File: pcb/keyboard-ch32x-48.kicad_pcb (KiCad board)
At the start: 2 copper layers, 224.6 x 74.2 mm, 116 parts, among them J1 USB_C_Receptacle_USB2.0, J2 Conn_01x02, J3 Conn_01x04, SW1 SW_SPST, SW2 SW_SPST, U1 CH32X033F8P6

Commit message: pcb: ch32x-48: rev2025.2
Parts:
- added C3: 4.7uF, Capacitor_SMD:C_0805_2012Metric, B.Cu at (154.7, 64.5)
- turned D_1_1 to -90 degrees
- turned D_1_2 to -90 degrees
- turned D_1_3 to -90 degrees
- turned D_1_4 to -90 degrees
- turned D_1_5 to -90 degrees
- turned D_1_6 to -90 degrees
- turned D_1_7 to -90 degrees
- turned D_2_1 to -90 degrees
- turned D_2_2 to -90 degrees
- turned D_2_3 to -90 degrees
- turned D_2_4 to -90 degrees
- turned D_2_5 to -90 degrees
- turned D_2_6 to -90 degrees
- turned D_2_7 to -90 degrees
- turned D_3_1 to -90 degrees
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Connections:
- D_1_1 pad 1: /ROW1 -> Net-(D_1_1-K)
- D_1_1 pad 2: Net-(D_1_1-A) -> /ROW1
- D_1_2 pad 1: /ROW1 -> Net-(D_1_2-K)
- D_1_2 pad 2: Net-(D_1_2-A) -> /ROW1
- D_1_3 pad 1: /ROW1 -> Net-(D_1_3-K)
- D_1_3 pad 2: Net-(D_1_3-A) -> /ROW1
- D_1_4 pad 1: /ROW1 -> Net-(D_1_4-K)
- D_1_4 pad 2: Net-(D_1_4-A) -> /ROW1
- D_1_5 pad 1: /ROW1 -> Net-(D_1_5-K)
- D_1_5 pad 2: Net-(D_1_5-A) -> /ROW1
- D_1_6 pad 1: /ROW1 -> Net-(D_1_6-K)
- D_1_6 pad 2: Net-(D_1_6-A) -> /ROW1
- D_1_7 pad 1: /ROW1 -> Net-(D_1_7-K)
- D_1_7 pad 2: Net-(D_1_7-A) -> /ROW1
- D_2_1 pad 1: /DCK -> Net-(D_2_1-K)
- D_2_1 pad 2: Net-(D_2_1-A) -> /DCK
- D_2_2 pad 1: /DCK -> Net-(D_2_2-K)
- D_2_2 pad 2: Net-(D_2_2-A) -> /DCK
- D_2_3 pad 1: /DCK -> Net-(D_2_3-K)
- D_2_3 pad 2: Net-(D_2_3-A) -> /DCK
- D_2_4 pad 1: /DCK -> Net-(D_2_4-K)
- D_2_4 pad 2: Net-(D_2_4-A) -> /DCK
- D_2_5 pad 1: /DCK -> Net-(D_2_5-K)
- D_2_5 pad 2: Net-(D_2_5-A) -> /DCK
- D_2_6 pad 1: /DCK -> Net-(D_2_6-K)
- D_2_6 pad 2: Net-(D_2_6-A) -> /DCK
- D_2_7 pad 1: /DCK -> Net-(D_2_7-K)
- D_2_7 pad 2: Net-(D_2_7-A) -> /DCK
- D_3_1 pad 1: /ROW3 -> Net-(D_3_1-K)
- D_3_1 pad 2: Net-(D_3_1-A) -> /ROW3
- D_3_2 pad 1: /ROW3 -> Net-(D_3_2-K)
- D_3_2 pad 2: Net-(D_3_2-A) -> /ROW3
- D_3_3 pad 1: /ROW3 -> Net-(D_3_3-K)
- D_3_3 pad 2: Net-(D_3_3-A) -> /ROW3
- D_3_4 pad 1: /ROW3 -> Net-(D_3_4-K)
- D_3_4 pad 2: Net-(D_3_4-A) -> /ROW3
- D_3_5 pad 1: /ROW3 -> Net-(D_3_5-K)
- D_3_5 pad 2: Net-(D_3_5-A) -> /ROW3
- D_3_6 pad 1: /ROW3 -> Net-(D_3_6-K)
- D_3_6 pad 2: Net-(D_3_6-A) -> /ROW3
- D_3_7 pad 1: /ROW3 -> Net-(D_3_7-K)
- D_3_7 pad 2: Net-(D_3_7-A) -> /ROW3
- D_4_1 pad 1: /ROW4 -> Net-(D_4_1-K)
- D_4_1 pad 2: Net-(D_4_1-A) -> /ROW4
- D_4_2 pad 1: /ROW4 -> Net-(D_4_2-K)
- D_4_2 pad 2: Net-(D_4_2-A) -> /ROW4
- D_4_3 pad 1: /ROW4 -> Net-(D_4_3-K)
- D_4_3 pad 2: Net-(D_4_3-A) -> /ROW4
- D_4_4 pad 1: /ROW4 -> Net-(D_4_4-K)
- D_4_4 pad 2: Net-(D_4_4-A) -> /ROW4
- D_4_5 pad 1: /ROW4 -> Net-(D_4_5-K)
- D_4_5 pad 2: Net-(D_4_5-A) -> /ROW4
- D_4_6 pad 1: /ROW4 -> Net-(D_4_6-K)
- D_4_6 pad 2: Net-(D_4_6-A) -> /ROW4
- D_4_7 pad 1: /ROW4 -> Net-(D_4_7-K)
- D_4_7 pad 2: Net-(D_4_7-A) -> /ROW4
- D_5_1 pad 1: /ROW5 -> Net-(D_5_1-K)
- D_5_1 pad 2: Net-(D_5_1-A) -> /ROW5
- D_5_2 pad 1: /ROW5 -> Net-(D_5_2-K)
- D_5_2 pad 2: Net-(D_5_2-A) -> /ROW5
- D_5_3 pad 1: /ROW5 -> Net-(D_5_3-K)
- D_5_3 pad 2: Net-(D_5_3-A) -> /ROW5
- D_5_4 pad 1: /ROW5 -> Net-(D_5_4-K)
- D_5_4 pad 2: Net-(D_5_4-A) -> /ROW5
- D_5_5 pad 1: /ROW5 -> Net-(D_5_5-K)
- D_5_5 pad 2: Net-(D_5_5-A) -> /ROW5
- D_5_6 pad 1: /ROW5 -> Net-(D_5_6-K)
- D_5_6 pad 2: Net-(D_5_6-A) -> /ROW5
- D_5_7 pad 1: /ROW5 -> Net-(D_5_7-K)
- D_5_7 pad 2: Net-(D_5_7-A) -> /ROW5
- D_6_1 pad 1: /DIO -> Net-(D_6_1-K)
- D_6_1 pad 2: Net-(D_6_1-A) -> /DIO
- D_6_2 pad 1: /DIO -> Net-(D_6_2-K)
- D_6_2 pad 2: Net-(D_6_2-A) -> /DIO
- D_6_3 pad 1: /DIO -> Net-(D_6_3-K)
- D_6_3 pad 2: Net-(D_6_3-A) -> /DIO
- D_6_4 pad 1: /DIO -> Net-(D_6_4-K)
- D_6_4 pad 2: Net-(D_6_4-A) -> /DIO
- D_6_5 pad 1: /DIO -> Net-(D_6_5-K)
- D_6_5 pad 2: Net-(D_6_5-A) -> /DIO
- D_6_6 pad 1: /DIO -> Net-(D_6_6-K)
- D_6_6 pad 2: Net-(D_6_6-A) -> /DIO
- D_6_7 pad 1: /DIO -> Net-(D_6_7-K)
- D_6_7 pad 2: Net-(D_6_7-A) -> /DIO
- D_7_1 pad 1: /ROW7 -> Net-(D_7_1-K)
- D_7_1 pad 2: Net-(D_7_1-A) -> /ROW7
- D_7_2 pad 1: /ROW7 -> Net-(D_7_2-K)
- D_7_2 pad 2: Net-(D_7_2-A) -> /ROW7
- D_7_3 pad 1: /ROW7 -> Net-(D_7_3-K)
- D_7_3 pad 2: Net-(D_7_3-A) -> /ROW7
- D_7_4 pad 1: /ROW7 -> Net-(D_7_4-K)
- D_7_4 pad 2: Net-(D_7_4-A) -> /ROW7
- D_7_5 pad 1: /ROW7 -> Net-(D_7_5-K)
- D_7_5 pad 2: Net-(D_7_5-A) -> /ROW7
- D_7_6 pad 1: /ROW7 -> Net-(D_7_6-K)
- D_7_6 pad 2: Net-(D_7_6-A) -> /ROW7
- SW_1_1 pad 2: Net-(D_1_1-A) -> Net-(D_1_1-K)
- SW_1_2 pad 2: Net-(D_1_2-A) -> Net-(D_1_2-K)
- SW_1_3 pad 2: Net-(D_1_3-A) -> Net-(D_1_3-K)
- SW_1_4 pad 2: Net-(D_1_4-A) -> Net-(D_1_4-K)
- SW_1_5 pad 2: Net-(D_1_5-A) -> Net-(D_1_5-K)
- SW_1_6 pad 2: Net-(D_1_6-A) -> Net-(D_1_6-K)
- SW_1_7 pad 2: Net-(D_1_7-A) -> Net-(D_1_7-K)
- SW_2_1 pad 2: Net-(D_2_1-A) -> Net-(D_2_1-K)
- SW_2_2 pad 2: Net-(D_2_2-A) -> Net-(D_2_2-K)
- SW_2_3 pad 2: Net-(D_2_3-A) -> Net-(D_2_3-K)
- SW_2_4 pad 2: Net-(D_2_4-A) -> Net-(D_2_4-K)
- SW_2_5 pad 2: Net-(D_2_5-A) -> Net-(D_2_5-K)
- SW_2_6 pad 2: Net-(D_2_6-A) -> Net-(D_2_6-K)
- SW_2_7 pad 2: Net-(D_2_7-A) -> Net-(D_2_7-K)
- SW_3_1 pad 2: Net-(D_3_1-A) -> Net-(D_3_1-K)
- SW_3_2 pad 2: Net-(D_3_2-A) -> Net-(D_3_2-K)
- SW_3_3 pad 2: Net-(D_3_3-A) -> Net-(D_3_3-K)
- SW_3_4 pad 2: Net-(D_3_4-A) -> Net-(D_3_4-K)
- SW_3_5 pad 2: Net-(D_3_5-A) -> Net-(D_3_5-K)
- SW_3_6 pad 2: Net-(D_3_6-A) -> Net-(D_3_6-K)
- SW_3_7 pad 2: Net-(D_3_7-A) -> Net-(D_3_7-K)
- SW_4_1 pad 2: Net-(D_4_1-A) -> Net-(D_4_1-K)
- SW_4_2 pad 2: Net-(D_4_2-A) -> Net-(D_4_2-K)
- SW_4_3 pad 2: Net-(D_4_3-A) -> Net-(D_4_3-K)
- SW_4_4 pad 2: Net-(D_4_4-A) -> Net-(D_4_4-K)
- SW_4_5 pad 2: Net-(D_4_5-A) -> Net-(D_4_5-K)
- SW_4_6 pad 2: Net-(D_4_6-A) -> Net-(D_4_6-K)
- SW_4_7 pad 2: Net-(D_4_7-A) -> Net-(D_4_7-K)
- SW_5_1 pad 2: Net-(D_5_1-A) -> Net-(D_5_1-K)
- SW_5_2 pad 2: Net-(D_5_2-A) -> Net-(D_5_2-K)
- SW_5_3 pad 2: Net-(D_5_3-A) -> Net-(D_5_3-K)
- SW_5_4 pad 2: Net-(D_5_4-A) -> Net-(D_5_4-K)
- SW_5_5 pad 2: Net-(D_5_5-A) -> Net-(D_5_5-K)
- SW_5_6 pad 2: Net-(D_5_6-A) -> Net-(D_5_6-K)
- SW_5_7 pad 2: Net-(D_5_7-A) -> Net-(D_5_7-K)
- SW_6_1 pad 2: Net-(D_6_1-A) -> Net-(D_6_1-K)
- SW_6_2 pad 2: Net-(D_6_2-A) -> Net-(D_6_2-K)
- SW_6_3 pad 2: Net-(D_6_3-A) -> Net-(D_6_3-K)
- SW_6_4 pad 2: Net-(D_6_4-A) -> Net-(D_6_4-K)
- SW_6_5 pad 2: Net-(D_6_5-A) -> Net-(D_6_5-K)
- SW_6_6 pad 2: Net-(D_6_6-A) -> Net-(D_6_6-K)
- SW_6_7 pad 2: Net-(D_6_7-A) -> Net-(D_6_7-K)
- SW_7_1 pad 2: Net-(D_7_1-A) -> Net-(D_7_1-K)
- SW_7_2 pad 2: Net-(D_7_2-A) -> Net-(D_7_2-K)
- SW_7_3 pad 2: Net-(D_7_3-A) -> Net-(D_7_3-K)
- SW_7_4 pad 2: Net-(D_7_4-A) -> Net-(D_7_4-K)
- SW_7_5 pad 2: Net-(D_7_5-A) -> Net-(D_7_5-K)
- SW_7_6 pad 2: Net-(D_7_6-A) -> Net-(D_7_6-K)
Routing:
- net Net-(D_2_4-K): track 0.00 -> 14.5 mm
- net Net-(D_2_4-A): track 14.5 -> 0.00 mm
- net Net-(D_7_3-K): track 0.00 -> 12.1 mm
- net Net-(D_7_3-A): track 12.1 -> 0.00 mm
- net Net-(D_2_5-K): track 0.00 -> 12.1 mm
- net Net-(D_2_5-A): track 12.1 -> 0.00 mm
- net Net-(D_1_4-K): track 0.00 -> 12.1 mm
- net Net-(D_1_4-A): track 12.1 -> 0.00 mm
- net Net-(D_1_3-K): track 0.00 -> 12.1 mm
- net Net-(D_1_3-A): track 12.1 -> 0.00 mm
- net Net-(D_1_2-K): track 0.00 -> 12.1 mm
- net Net-(D_1_2-A): track 12.1 -> 0.00 mm
- net Net-(D_6_2-K): track 0.00 -> 12.1 mm
- net Net-(D_6_2-A): track 12.1 -> 0.00 mm
- net Net-(D_5_1-K): track 0.00 -> 12.1 mm
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
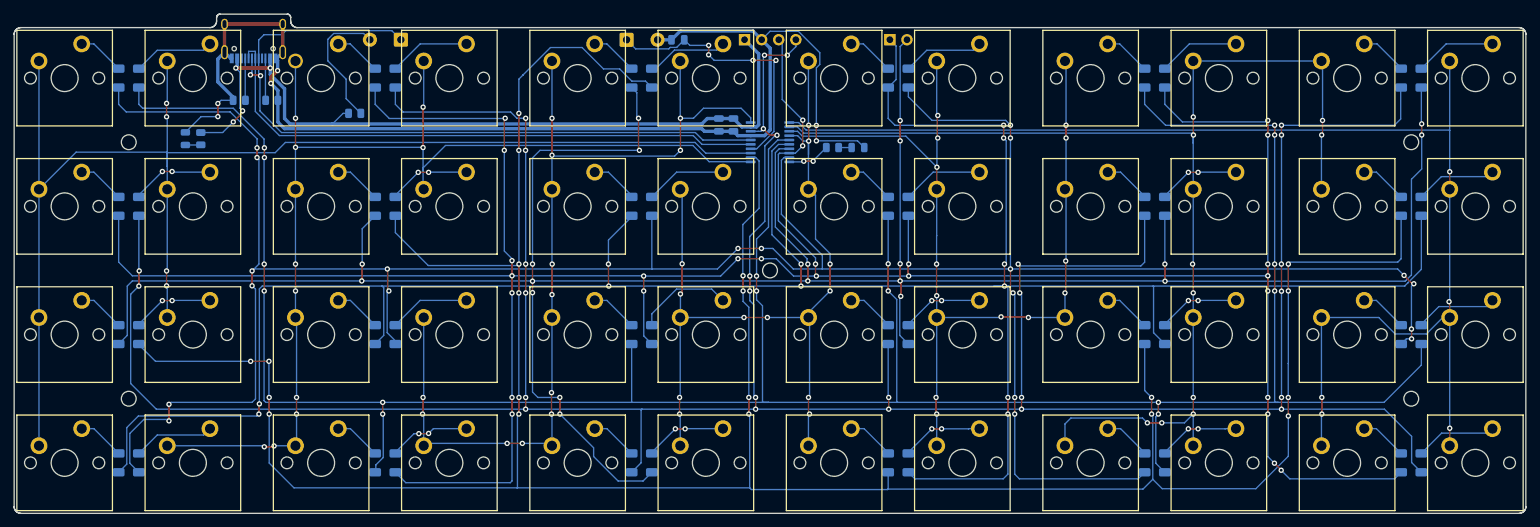
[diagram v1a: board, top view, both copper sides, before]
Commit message: pcb: ch32x-48 rev2025.3
rev2025.3:
- increase trace width to 0.25,
  - fix DRC.
- add 10K pullup for Row6 (DIO),
   per testing of the rev2025.1 board.

rev2025.2:
- fixed the diodes to be col2row,
  as the assignments of rows
  (and CH32X limitations on pins)
  required this.
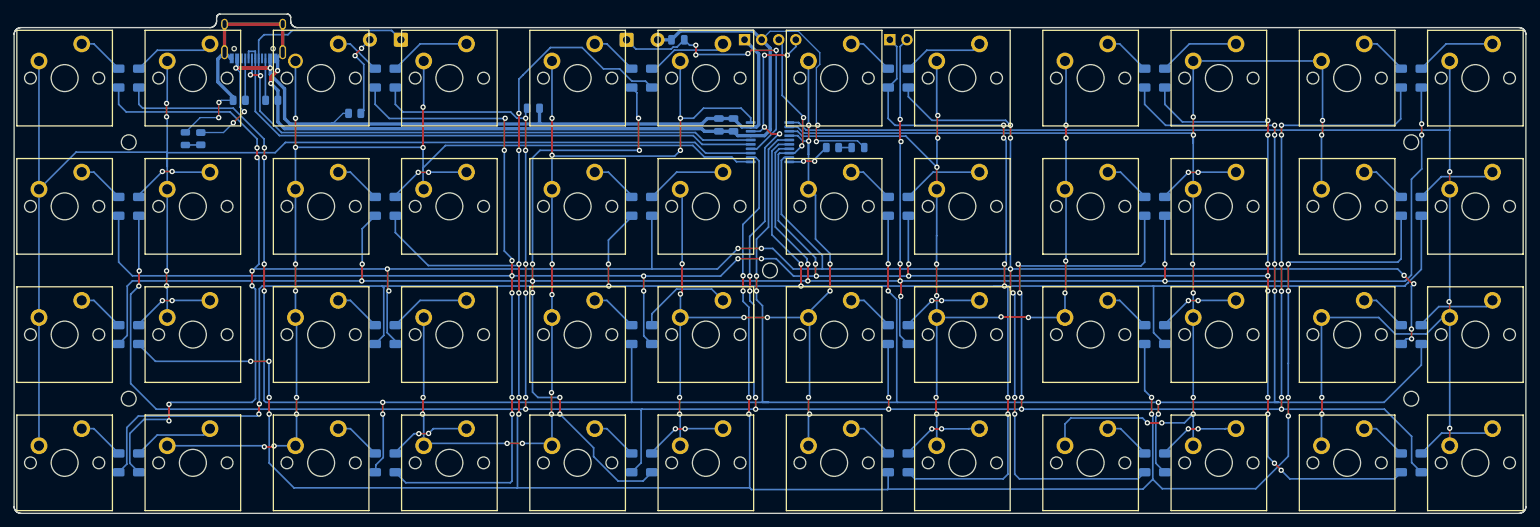
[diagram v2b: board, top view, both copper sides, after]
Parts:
- added R6: 10K, Resistor_SMD:R_0805_2012Metric, B.Cu at (127.1, 62.0)
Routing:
- net Net-(SW2-B): track 20.0 -> 12.6 mm, vias 0 -> 2
- net /VDD: track 119.2 -> 121.9 mm
- net /DIO: track 487.8 -> 490.0 mm
- net /RESET: track 40.6 -> 42.2 mm

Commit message: pcb: ch32x-48 rev2025.4
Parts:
- removed R6: 10K, Resistor_SMD:R_0805_2012Metric
- SW_1_1, SW_1_2, SW_1_3, SW_1_4, SW_1_5, SW_1_6, SW_1_7, SW_2_1, SW_2_2, SW_2_3, SW_2_4, SW_2_5, SW_2_6, SW_2_7, SW_3_1, SW_3_2, SW_3_3, SW_3_4, SW_3_5, SW_3_6, SW_3_7, SW_4_1, SW_4_2, SW_4_3, SW_4_4, SW_4_5, SW_4_6, SW_4_7, SW_5_1, SW_5_2, SW_5_3, SW_5_4, SW_5_5, SW_5_6, SW_5_7, SW_6_1, SW_6_2, SW_6_3, SW_6_4, SW_6_5, SW_6_6, SW_6_7, SW_7_1, SW_7_2, SW_7_3, SW_7_4, SW_7_5, SW_7_6: value MX-compatible or Kailh Choc v1 -> MX-compatible
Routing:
- net /VDD: track 121.9 -> 119.5 mm
- net /DIO: track 490.0 -> 488.5 mm
